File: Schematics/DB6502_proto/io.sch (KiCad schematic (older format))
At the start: 23 parts, among them J7 UART A, J8 UART B, J9 UART_A, U18 SC26C92, U19 FT230XS, U2 74AC32, U5 74AC04, Y2 3,6864MHz

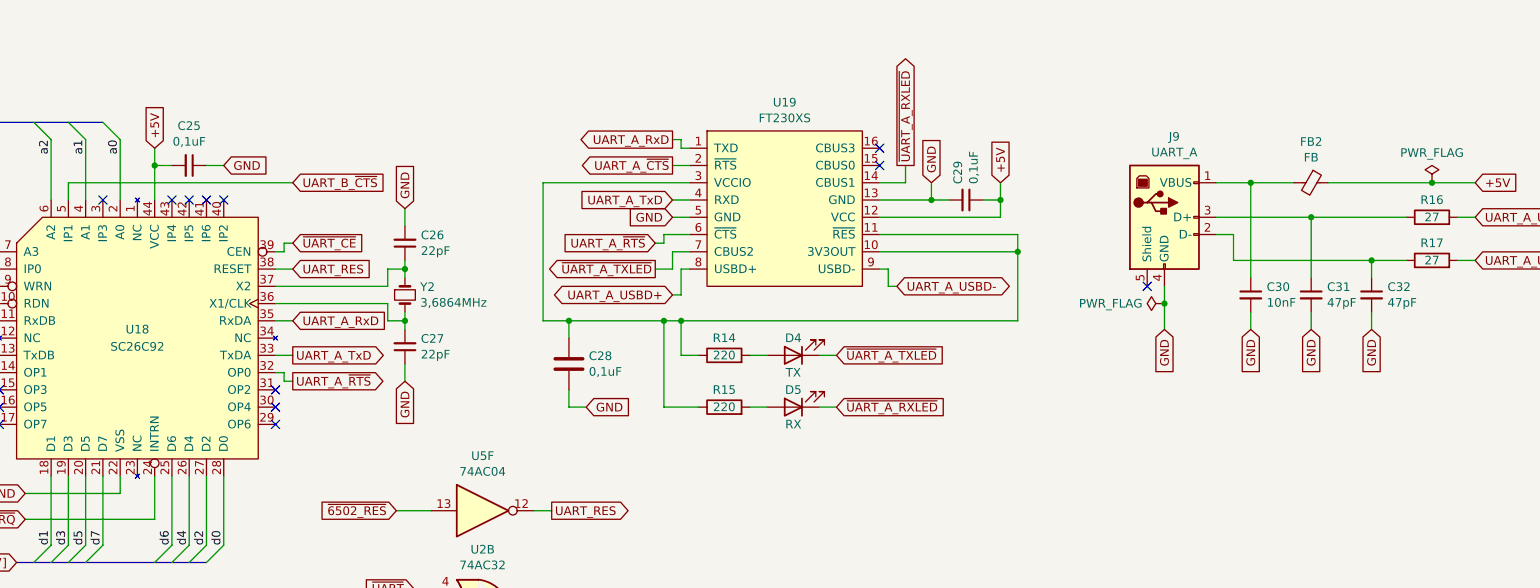
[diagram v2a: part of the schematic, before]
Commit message: Implemented fix for metastability issue during clock switch
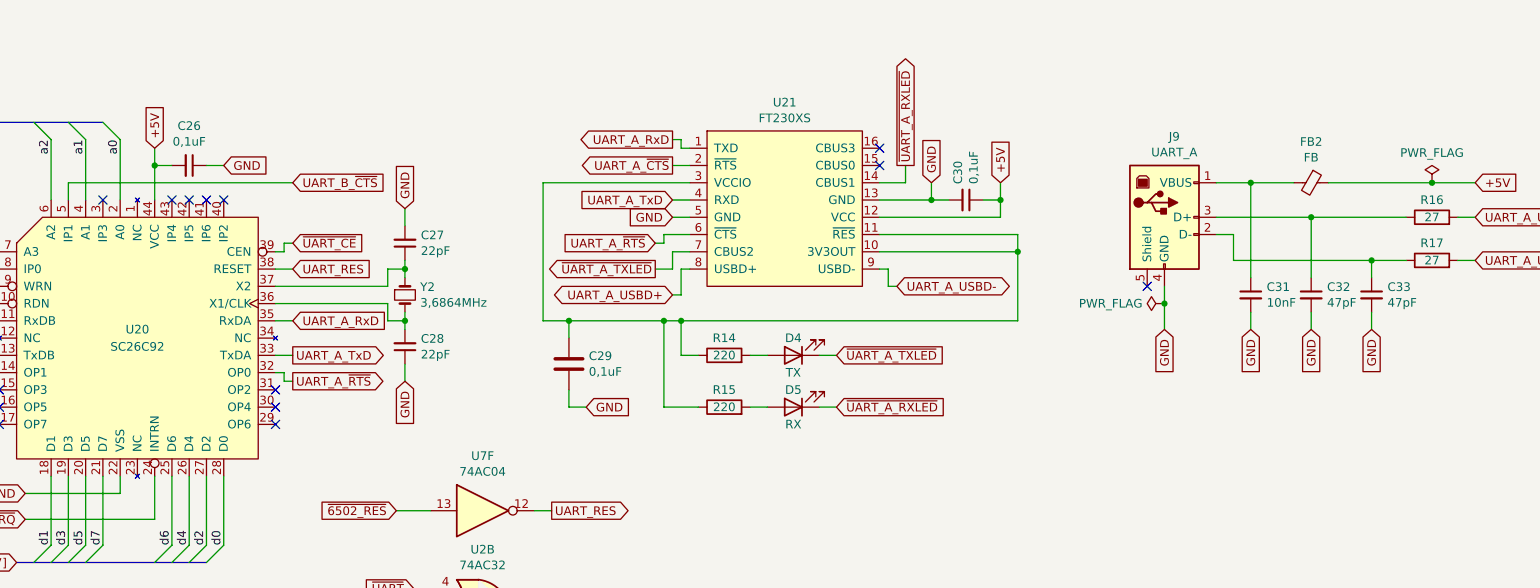
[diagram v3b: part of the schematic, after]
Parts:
- renumbered C25 to C26, C26 to C27, C27 to C28, C28 to C29, C29 to C30, C30 to C31, C31 to C32, C32 to C33, U18 to U20, U19 to U21, U5 to U7
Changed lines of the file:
@@
 $EndDescr
 $Comp
-L 6502:SC26C92 U18
+L 6502:SC26C92 U20
 U 1 1 5F92CA23
 P 2400 2050
-F 0 "U18" H 2400 2100 50  0000 C CNN
+F 0 "U20" H 2400 2100 50  0000 C CNN
 F 1 "SC26C92" H 2400 2000 50  0000 C CNN
 F 2 "" H 2400 2050 50  0001 C CNN
@@
 	2500 950  2500 1050
 $Comp
-L Device:C_Small C25
+L Device:C_Small C26
 U 1 1 5F932BB1
 P 2700 1050
-F 0 "C25" V 2471 1050 50  0000 C CNN
+F 0 "C26" V 2471 1050 50  0000 C CNN
 F 1 "0,1uF" V 2562 1050 50  0000 C CNN
 F 2 "" H 2700 1050 50  0001 C CNN
@@
 $EndComp
 $Comp
-L Device:C_Small C26
+L Device:C_Small C27
 U 1 1 5F93E98E
 P 3950 1500
-F 0 "C26" H 3858 1454 50  0000 R CNN
+F 0 "C27" H 3858 1454 50  0000 R CNN
 F 1 "22pF" H 3858 1545 50  0000 R CNN
 F 2 "" H 3950 1500 50  0001 C CNN
@@
 $EndComp
 $Comp
-L Device:C_Small C27
+L Device:C_Small C28
 U 1 1 5F93F1BF
 P 3950 2100
-F 0 "C27" H 3858 2054 50  0000 R CNN
+F 0 "C28" H 3858 2054 50  0000 R CNN
 F 1 "22pF" H 3858 2145 50  0000 R CNN
 F 2 "" H 3950 2100 50  0001 C CNN
@@
 AR Path="/6014B4D9/5F95BFD2" Ref="U?"  Part="1"
 AR Path="/5F8F4E1E/5F95BFD2" Ref="U?"  Part="1"
-AR Path="/5F910E81/5F95BFD2" Ref="U19"  Part="1"
-F 0 "U19" H 6150 1915 50  0000 C CNN
+AR Path="/5F910E81/5F95BFD2" Ref="U21"  Part="1"
+F 0 "U21" H 6150 1915 50  0000 C CNN
 F 1 "FT230XS" H 6150 1824 50  0000 C CNN
 F 2 "Package_SO:SSOP-16_5.3x6.2mm_P0.65mm" H 6150 1800 50  0001 C CNN
@@
 AR Path="/6014B4D9/5F95BFF2" Ref="C?"  Part="1"
 AR Path="/5F8F4E1E/5F95BFF2" Ref="C?"  Part="1"
-AR Path="/5F910E81/5F95BFF2" Ref="C28"  Part="1"
-F 0 "C28" H 5015 2246 50  0000 L CNN
+AR Path="/5F910E81/5F95BFF2" Ref="C29"  Part="1"
+F 0 "C29" H 5015 2246 50  0000 L CNN
 F 1 "0,1uF" H 5015 2155 50  0000 L CNN
 F 2 "Capacitor_THT:C_Disc_D5.0mm_W2.5mm_P2.50mm" H 4938 2050 50  0001 C CNN
@@
 P 7200 1250
 AR Path="/5F8F4E1E/5F95C03D" Ref="C?"  Part="1"
-AR Path="/5F910E81/5F95C03D" Ref="C29"  Part="1"
-F 0 "C29" H 7108 1204 50  0000 R CNN
+AR Path="/5F910E81/5F95C03D" Ref="C30"  Part="1"
+F 0 "C30" H 7108 1204 50  0000 R CNN
 F 1 "0,1uF" H 7108 1295 50  0000 R CNN
 F 2 "" H 7200 1250 50  0001 C CNN
@@
 AR Path="/6014B4D9/5F982938" Ref="C?"  Part="1"
 AR Path="/5F8F4E1E/5F982938" Ref="C?"  Part="1"
-AR Path="/5F910E81/5F982938" Ref="C31"  Part="1"
-F 0 "C31" H 9292 1846 50  0000 L CNN
+AR Path="/5F910E81/5F982938" Ref="C32"  Part="1"
+F 0 "C32" H 9292 1846 50  0000 L CNN
 F 1 "47pF" H 9292 1755 50  0000 L CNN
 F 2 "Capacitor_THT:C_Disc_D5.0mm_W2.5mm_P2.50mm" H 9200 1800 50  0001 C CNN
@@
 AR Path="/6014B4D9/5F98293E" Ref="C?"  Part="1"
 AR Path="/5F8F4E1E/5F98293E" Ref="C?"  Part="1"
-AR Path="/5F910E81/5F98293E" Ref="C32"  Part="1"
-F 0 "C32" H 9642 1846 50  0000 L CNN
+AR Path="/5F910E81/5F98293E" Ref="C33"  Part="1"
+F 0 "C33" H 9642 1846 50  0000 L CNN
 F 1 "47pF" H 9642 1755 50  0000 L CNN
 F 2 "Capacitor_THT:C_Disc_D5.0mm_W2.5mm_P2.50mm" H 9550 1800 50  0001 C CNN
@@
 AR Path="/6014B4D9/5F982950" Ref="C?"  Part="1"
 AR Path="/5F8F4E1E/5F982950" Ref="C?"  Part="1"
-AR Path="/5F910E81/5F982950" Ref="C30"  Part="1"
-F 0 "C30" H 8942 1846 50  0000 L CNN
+AR Path="/5F910E81/5F982950" Ref="C31"  Part="1"
+F 0 "C31" H 8942 1846 50  0000 L CNN
 F 1 "10nF" H 8942 1755 50  0000 L CNN
 F 2 "Capacitor_THT:C_Disc_D5.0mm_W2.5mm_P2.50mm" H 8850 1800 50  0001 C CNN
@@
 P 4400 3050
 AR Path="/5F8F4E1E/5F9A15C7" Ref="U?"  Part="6"
-AR Path="/5F910E81/5F9A15C7" Ref="U5"  Part="6"
-F 0 "U5" H 4400 3367 50  0000 C CNN
+AR Path="/5F910E81/5F9A15C7" Ref="U7"  Part="6"
+F 0 "U7" H 4400 3367 50  0000 C CNN
 F 1 "74AC04" H 4400 3276 50  0000 C CNN
 F 2 "" H 4400 3050 50  0001 C CNN

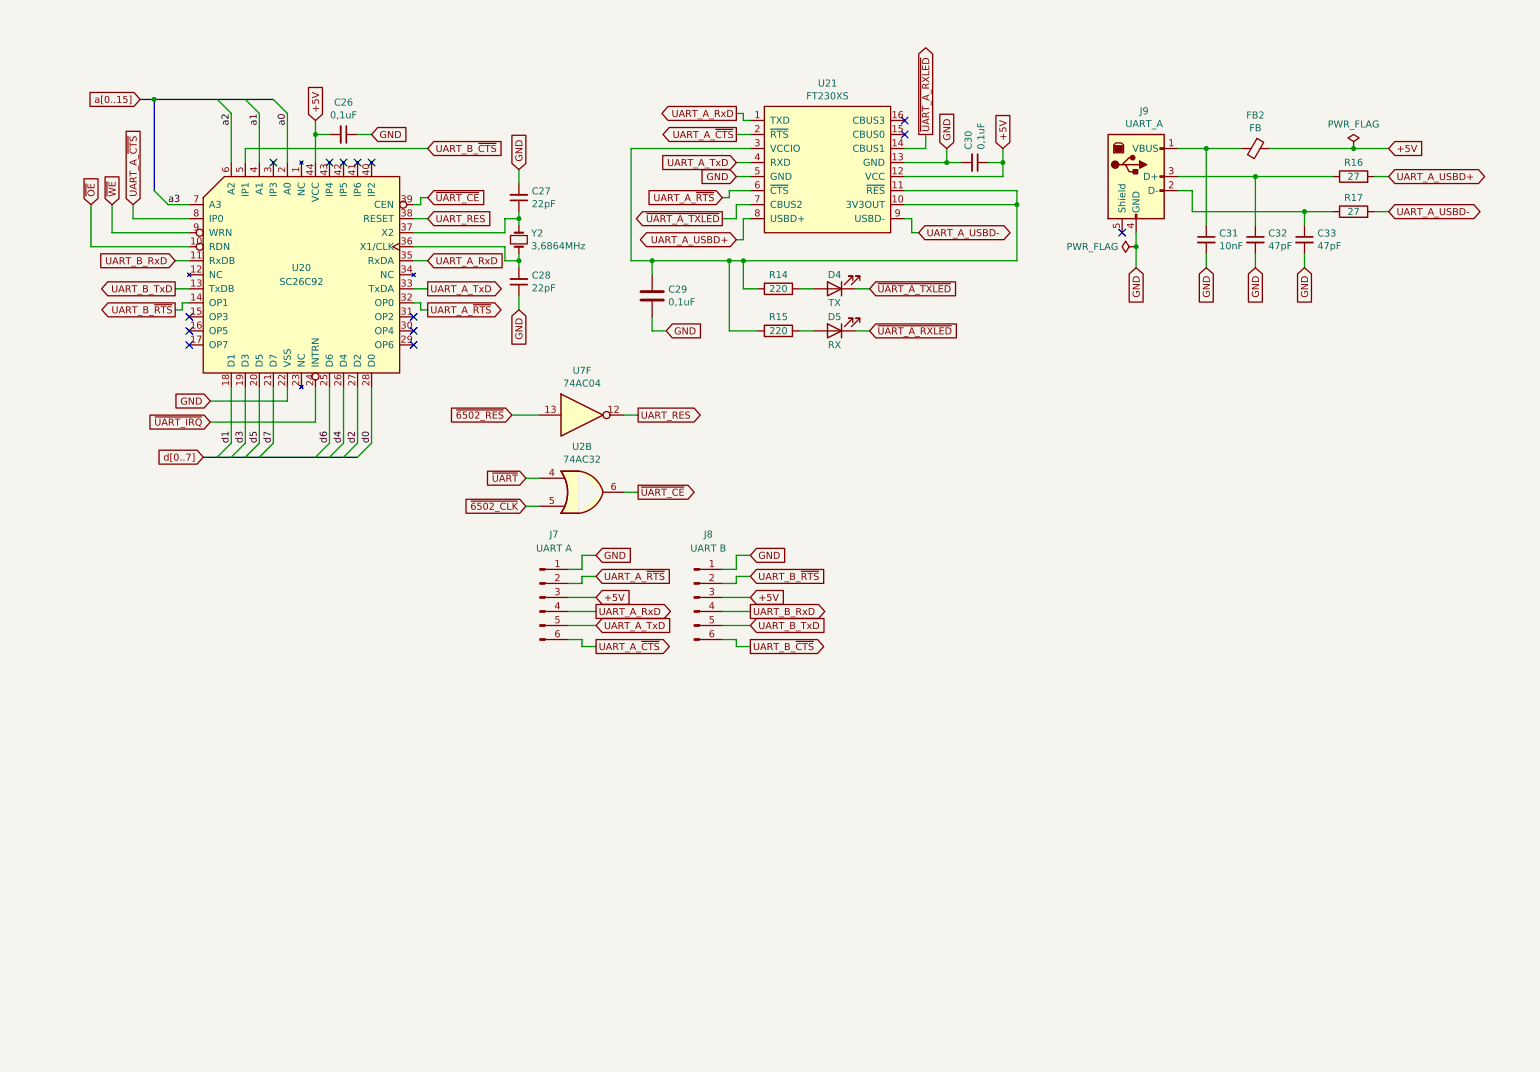
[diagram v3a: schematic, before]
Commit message: Added jumpers for serial source selection
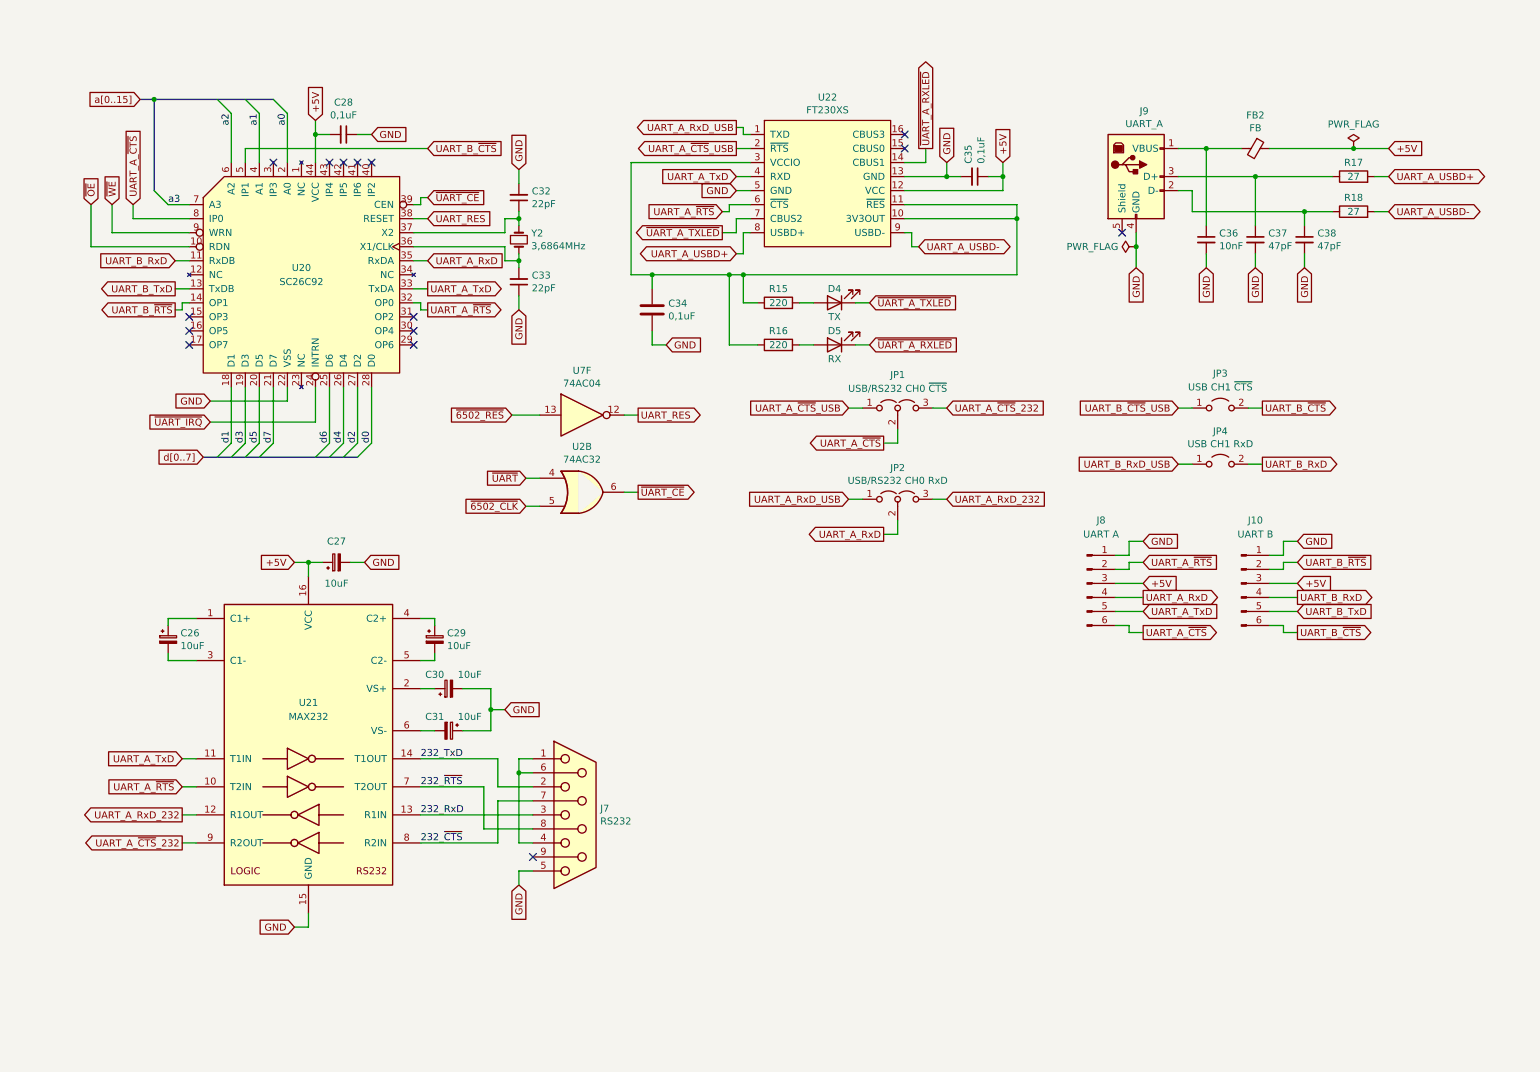
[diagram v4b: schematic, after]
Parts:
- added C26, C27, C29, C30, C31: 10uF, symbol Device:CP_Small
- added J7: RS232, symbol Connector:DB9_Female
- added JP1: USB/RS232 CH0 ~CTS, symbol Jumper:Jumper_3_Open
- added JP2: USB/RS232 CH0 RxD, symbol Jumper:Jumper_3_Open
- added JP3: USB CH1 ~CTS, symbol Jumper:Jumper_2_Open
- added JP4: USB CH1 RxD, symbol Jumper:Jumper_2_Open
- added U21: MAX232, symbol Interface_UART:MAX232
- renumbered C26 to C28, C27 to C32, C28 to C33, C29 to C34, C30 to C35, C31 to C36, C32 to C37, C33 to C38, J8 to J10, J7 to J8, R14 to R15, R15 to R16, R16 to R17, R17 to R18, U21 to U22
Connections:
- net +5V: now also C27.1, U21.16 (VCC)
- net GND: now also C27.2, C30.2, C31.1, J7.5, U21.15 (GND)
- net UART_A_RxD: now also JP2.2 (C); no longer U22.1 (TXD)
- net UART_A_TxD: now also U21.11 (T1IN)
- net UART_A_~CTS: now also JP1.2 (C); no longer U22.2 (~RTS)
- net UART_A_~RTS: now also U21.10 (T2IN)
- net UART_B_RxD: now also JP4.2 (B)
- net UART_B_~CTS: now also JP3.2 (B)
- new net: C26.1, U21.1 (C1+)
- new net: C30.1, U21.2 (VS+)
- new net: C26.2, U21.3 (C1-)
- new net: C29.1, U21.4 (C2+)
- new net: C29.2, U21.5 (C2-)
- new net: C31.2, U21.6 (VS-)
- new net: J7.1, J7.4, J7.6
- new net 232_RxD: J7.3, U21.13 (R1IN)
- new net 232_TxD: J7.2, U21.14 (T1OUT)
- new net 232_~CTS: J7.7, U21.8 (R2IN)
- new net 232_~RTS: J7.8, U21.7 (T2OUT)
- new net UART_A_RxD_232: JP2.3 (B), U21.12 (R1OUT)
- new net UART_A_RxD_USB: JP2.1 (A), U22.1 (TXD)
- new net UART_A_~CTS~_232: JP1.3 (B), U21.9 (R2OUT)
- new net UART_A_~CTS~_USB: JP1.1 (A), U22.2 (~RTS)
- new net UART_B_RxD_USB: JP4.1 (A)
- new net UART_B_~CTS~_USB: JP3.1 (A)
- no-connect marks 14 -> 15
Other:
- moved on the sheet: C34, C35, D4, D5, J10, J8, R15, R16, U22

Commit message: Added second USB channel to UART
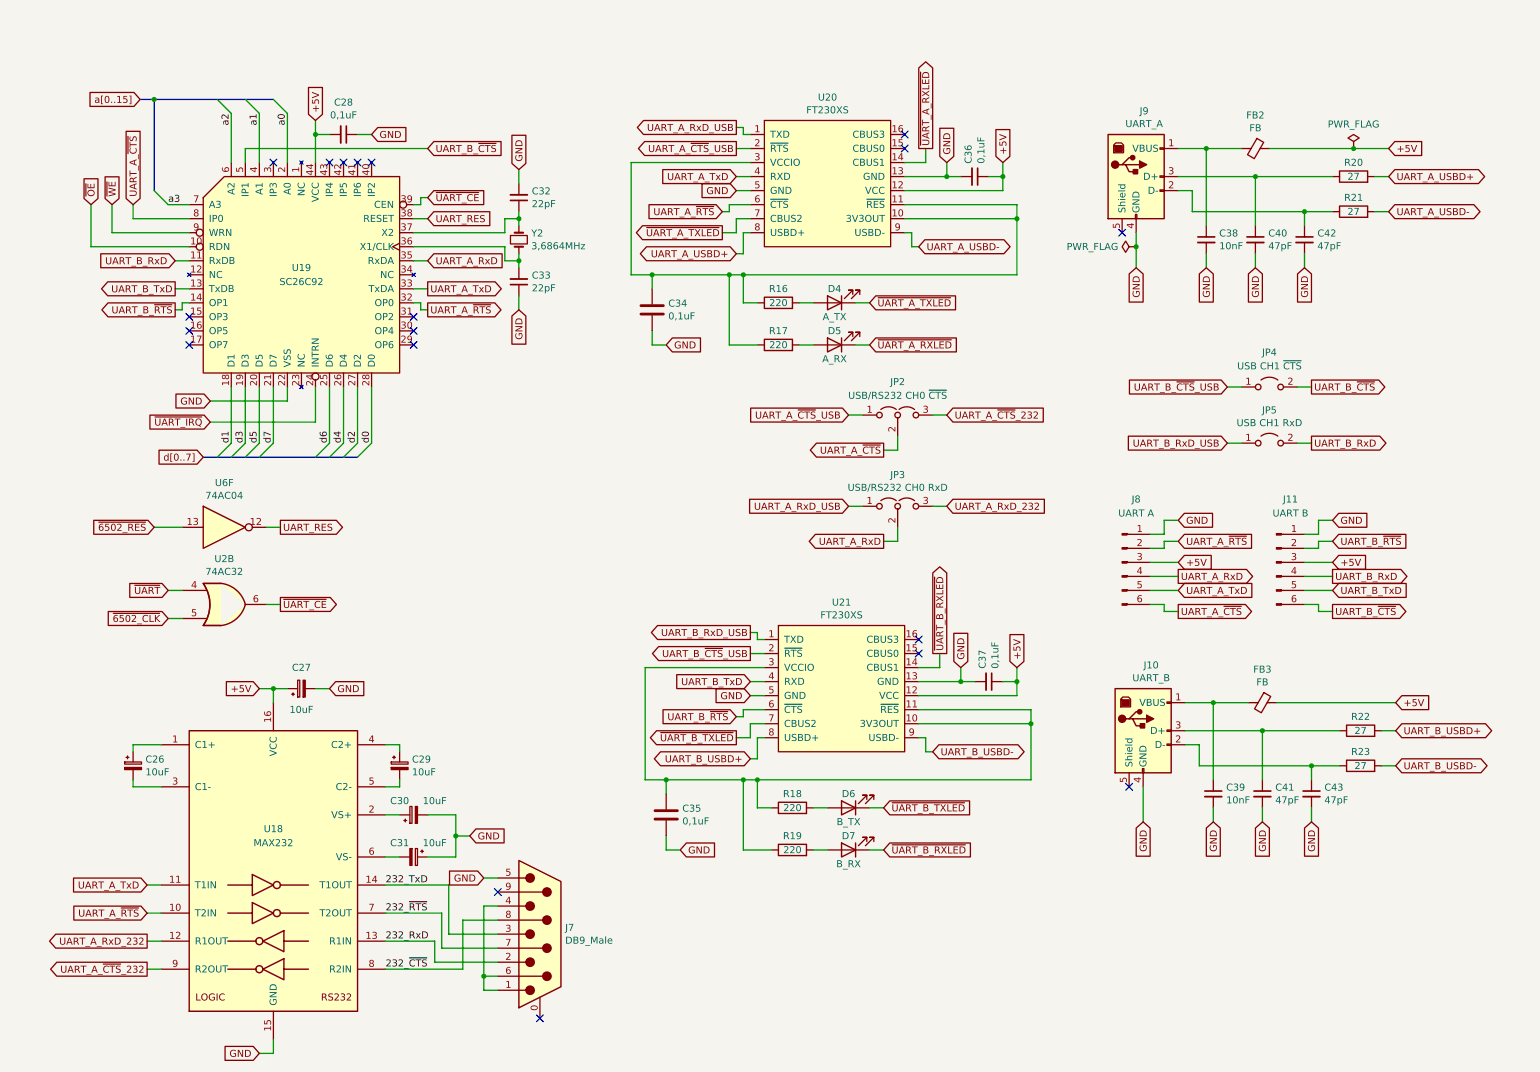
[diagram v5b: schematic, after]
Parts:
- removed J7: RS232, symbol Connector:DB9_Female
- added C35: 0,1uF, Capacitor_THT:C_Disc_D5.0mm_W2.5mm_P2.50mm, symbol Device:C
- added C37: 0,1uF, Capacitor_THT:C_Disc_D5.0mm_W2.5mm_P2.50mm, symbol Device:C_Small
- added C39: 10nF, Capacitor_THT:C_Disc_D5.0mm_W2.5mm_P2.50mm, symbol Device:C_Small
- added C41, C43: 47pF, Capacitor_THT:C_Disc_D5.0mm_W2.5mm_P2.50mm, symbol Device:C_Small
- added D6: B_TX, LED_THT:LED_D3.0mm, symbol Device:LED
- added D7: B_RX, LED_THT:LED_D3.0mm, symbol Device:LED
- added FB3: FB, Resistor_THT:R_Axial_DIN0207_L6.3mm_D2.5mm_P10.16mm_Horizontal, symbol Device:Ferrite_Bead_Small
- added J10: UART_B, Connector_USB:USB_B_OST_USB-B1HSxx_Horizontal, symbol 6502:USB_B
- added J7: DB9_Male, Connector_Dsub:DSUB-9_Male_Horizontal_P2.77x2.84mm_EdgePinOffset7.70mm_Housed_MountingHolesOffset9.12mm, symbol Connector:DB9_Male_MountingHoles
- added R18, R19: 220, Resistor_THT:R_Axial_DIN0207_L6.3mm_D2.5mm_P10.16mm_Horizontal, symbol Device:R
- added R22, R23: 27, Resistor_THT:R_Axial_DIN0207_L6.3mm_D2.5mm_P10.16mm_Horizontal, symbol Device:R
- added U21: FT230XS, Package_SO:SSOP-16_5.3x6.2mm_P0.65mm, symbol 6502:FT230XS
- C26, C27, C29, C30, C31: footprint (none) -> Capacitor_THT:CP_Radial_D4.0mm_P2.00mm
- C28, C32, C33: footprint (none) -> Capacitor_THT:C_Disc_D5.0mm_W2.5mm_P2.50mm
- C36: renamed from C35; footprint (none) -> Capacitor_THT:C_Disc_D5.0mm_W2.5mm_P2.50mm
- D4: value TX -> A_TX
- D5: value RX -> A_RX
- JP2: renamed from JP1; footprint (none) -> Connector_PinHeader_2.54mm:PinHeader_1x03_P2.54mm_Vertical
- JP3: renamed from JP2; footprint (none) -> Connector_PinHeader_2.54mm:PinHeader_1x03_P2.54mm_Vertical
- JP4: renamed from JP3; footprint (none) -> Connector_PinHeader_2.54mm:PinHeader_1x02_P2.54mm_Vertical
- JP5: renamed from JP4; footprint (none) -> Connector_PinHeader_2.54mm:PinHeader_1x02_P2.54mm_Vertical
- U18: renamed from U21; footprint (none) -> Package_DIP:DIP-16_W7.62mm_Socket
- U19: renamed from U20; footprint (none) -> Package_LCC:PLCC-44_THT-Socket
- U2: footprint (none) -> Package_DIP:DIP-14_W7.62mm_Socket
- U6: renamed from U7; footprint (none) -> Package_DIP:DIP-14_W7.62mm_Socket
- Y2: footprint (none) -> Crystal:Crystal_HC49-U_Vertical
- renumbered C36 to C38, C37 to C40, C38 to C42, J10 to J11, R15 to R16, R16 to R17, R17 to R20, R18 to R21, U22 to U20
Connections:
- net +5V: now also C37.1, FB3.1, U21.12 (VCC)
- net 232_RxD: now also J7.2
- net 232_TxD: now also J7.3
- net 232_~CTS: now also J7.8
- net 232_~RTS: now also J7.7
- net GND: now also C35.2, C37.2, C39.2, C41.2, C43.2, J10.4 (GND), J7.5, U21.13 (GND), U21.5 (GND)
- net UART_B_RxD_USB: now also U21.1 (TXD)
- net UART_B_TxD: now also U21.4 (RXD)
- net UART_B_~CTS~_USB: now also U21.2 (~RTS)
- net UART_B_~RTS: now also U21.6 (~CTS)
- new net: J7.1, J7.4, J7.6
- new net: C35.1, R18.1, R19.1, U21.10 (3V3OUT), U21.11 (~RES), U21.3 (VCCIO)
- new net: D6.2 (A), R18.2
- new net: D7.2 (A), R19.2
- new net: C39.1, FB3.2, J10.1 (VBUS)
- new net: C43.1, J10.2 (D-), R23.1
- new net: C41.1, J10.3 (D+), R22.1
- new net UART_B_USBD+: R22.2, U21.8 (USBD+)
- new net UART_B_USBD-: R23.2, U21.9 (USBD-)
- new net ~UART_B_RXLED: D7.1 (K), U21.14 (CBUS1)
- new net ~UART_B_TXLED: D6.1 (K), U21.7 (CBUS2)
- no-connect marks 15 -> 19
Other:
- moved on the sheet: C26, C27, C29, C30, C31, J11, J8, JP2, JP3, JP4, JP5, U18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
